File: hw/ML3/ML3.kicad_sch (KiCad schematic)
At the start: 6 parts, among them J1 Conn_01x07, J2 5-12V Supply

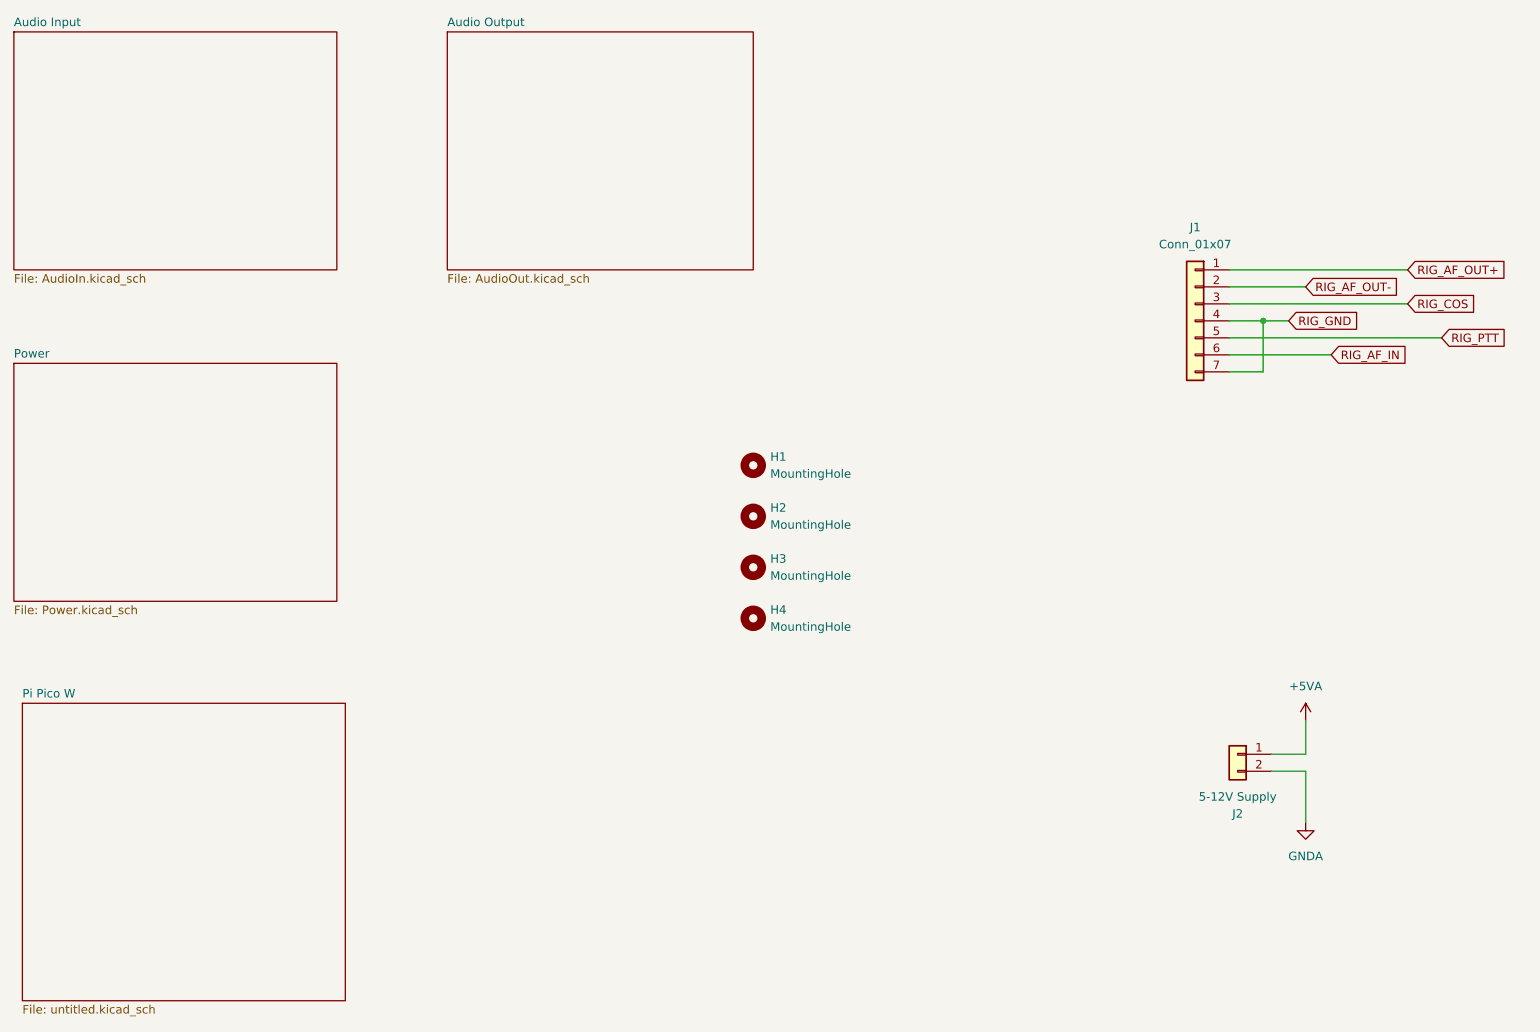
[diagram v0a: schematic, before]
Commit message: ML3 board modified for improved case/DFM.  Sending this version to Steve
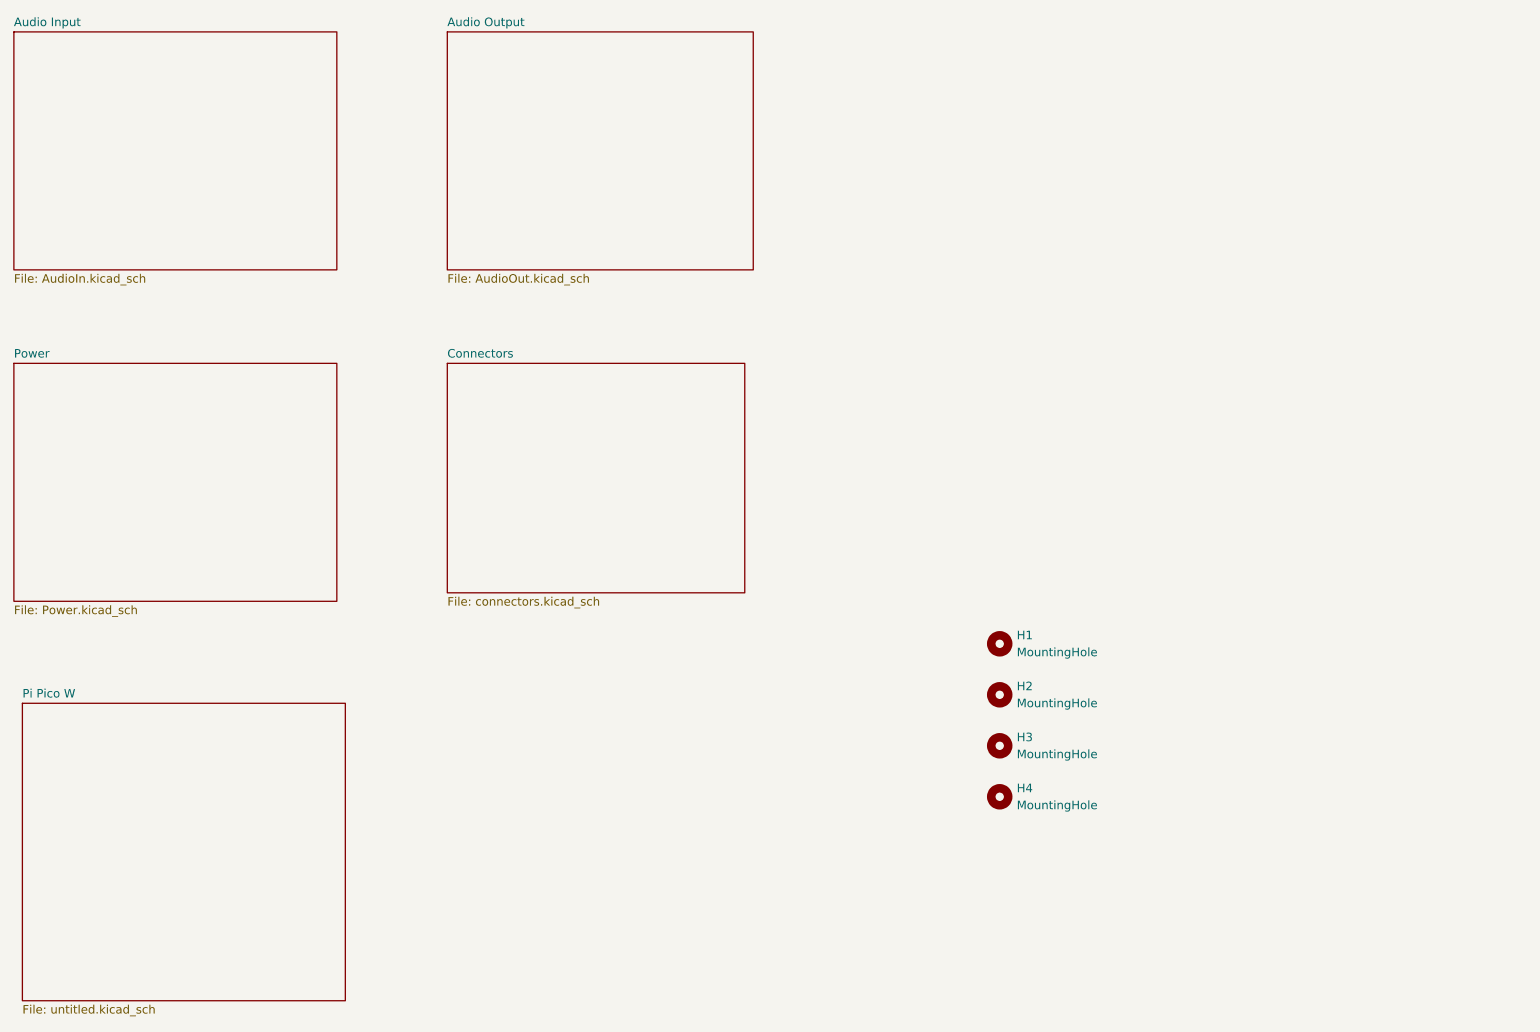
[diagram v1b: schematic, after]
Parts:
- removed J1: Conn_01x07, Connector_PinHeader_2.54mm:PinHeader_1x07_P2.54mm_Vertical, symbol Connector_Generic:Conn_01x07
- removed J2: 5-12V Supply, Connector_PinHeader_2.54mm:PinHeader_1x02_P2.54mm_Vertical, symbol Connector_Generic:Conn_01x02
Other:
- added sheet Connectors (connectors.kicad_sch)
- moved on the sheet: H1, H2, H3, H4
